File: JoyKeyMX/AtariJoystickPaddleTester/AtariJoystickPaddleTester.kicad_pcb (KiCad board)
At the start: 2 copper layers, 106.7 x 142.2 mm, 52 parts, among them J1 DB9_Male, J2 Barrel_Jack, SW1 SWITCH, U1 LM7809_TO220, U2 LM3914V, U3 LM3914V

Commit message: Route Atari Joystick and Paddle Tester
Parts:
- added G***: LOGO, Library:ScreamingLogo, F.Cu at (79.4, 87.6)
- added REF**: OSH_logo, Library:OSH_logo, F.Cu at (137.2, 168.8)
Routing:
- net 9V: track 0.00 -> 504.2 mm
- net GND: track 0.00 -> 238.8 mm, vias 0 -> 19
- net Net-(D11-Pad1): track 0.00 -> 197.8 mm
- net +9V: track 0.00 -> 185.4 mm
- net Net-(D10-Pad1): track 0.00 -> 180.4 mm
- net LEFT PADDLE & FIRE: track 0.00 -> 179.3 mm
- net Net-(D9-Pad1): track 0.00 -> 163.3 mm
- net Net-(D8-Pad1): track 0.00 -> 146.2 mm
- net Net-(D7-Pad1): track 0.00 -> 129.1 mm
- net 5V: track 0.00 -> 125.5 mm
- net Net-(D27-Pad1): track 0.00 -> 124.3 mm
- net RIGHT PADDLE & FIRE: track 0.00 -> 123.4 mm
- net Net-(D26-Pad1): track 0.00 -> 113.0 mm
- net Net-(D6-Pad1): track 0.00 -> 112.0 mm
- net Net-(D25-Pad1): track 0.00 -> 101.7 mm
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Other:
- board size 106.7 x 142.2 mm -> 106.7 x 144.8 mm
- board text added: "(c) Bertrand Le Roy 2022 https://github.com/bleroy/3d-junkyard/tree/main/JoyKeyMX https://atariage.com/forums/profile/76850-screamingattheradio/ https://www.twitch.tv/screamingattheradio https://www.youtube.com/channel/UCyaCK4oVWf1ty618W-MJcrg"
- board text added: "Atari Joystick and Paddle Tester"

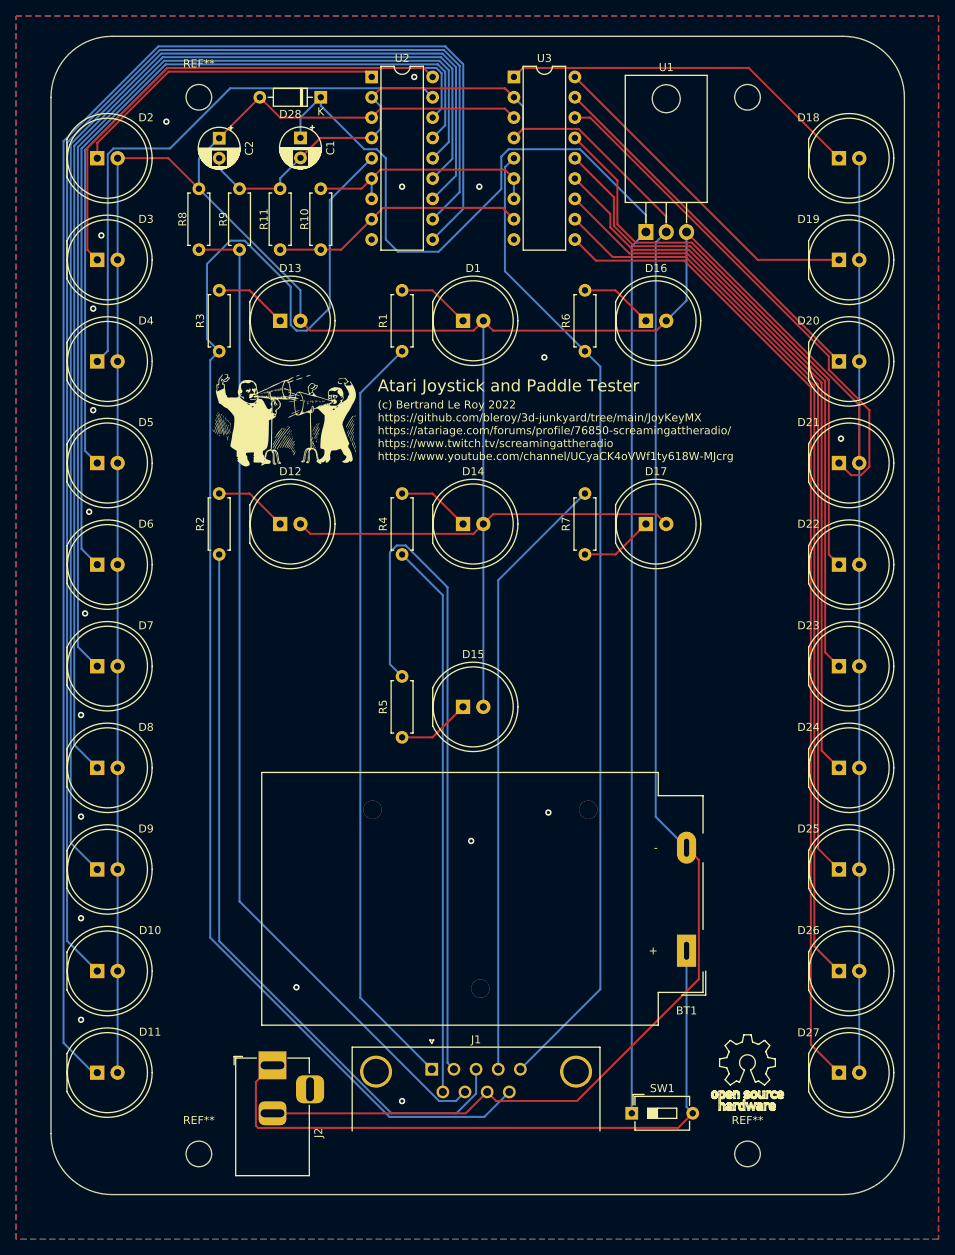
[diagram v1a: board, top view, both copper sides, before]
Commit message: Remove some unnecessary tracks.
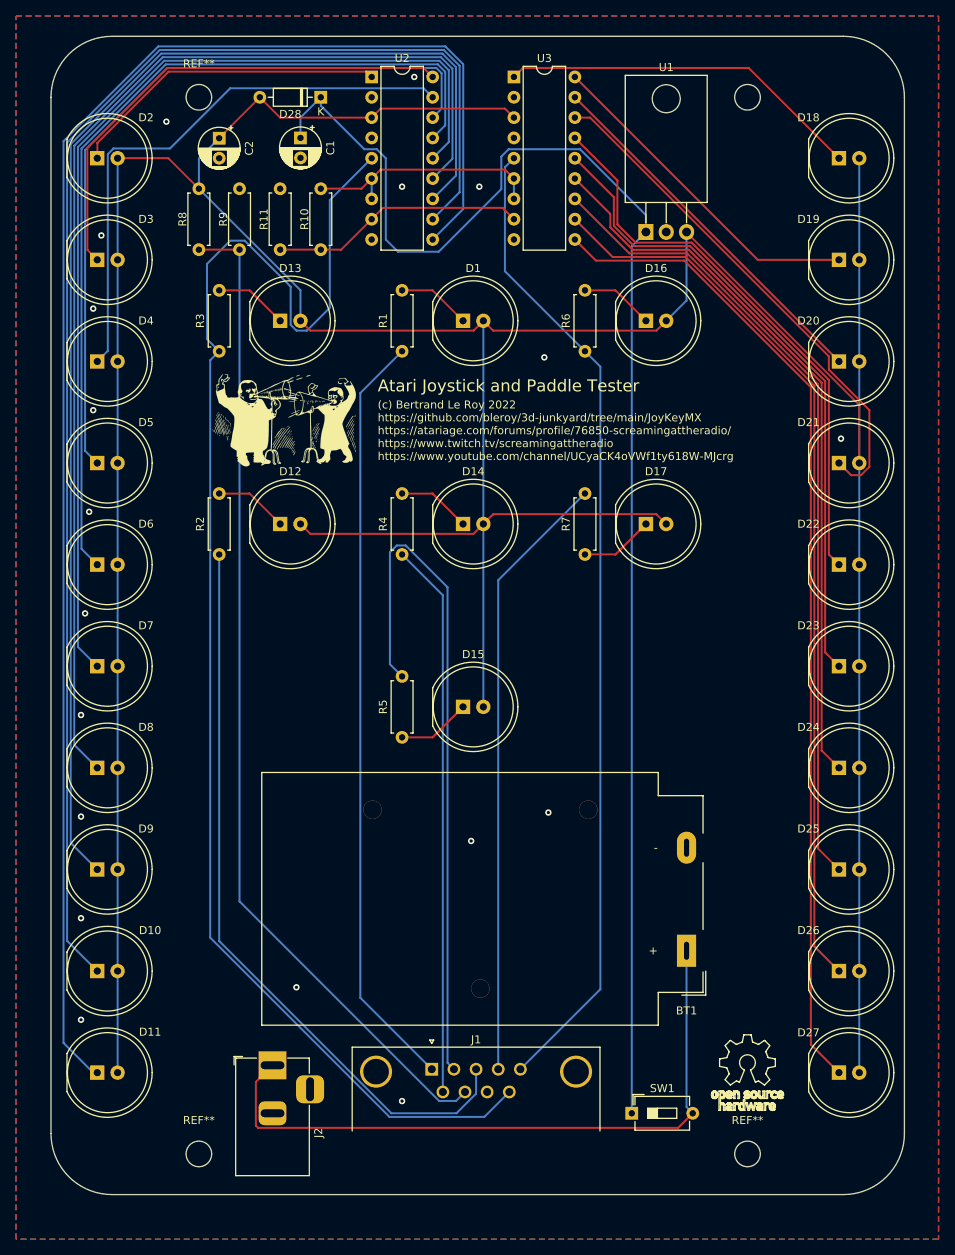
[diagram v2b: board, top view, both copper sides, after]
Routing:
- net GND: track 238.8 -> 0.00 mm
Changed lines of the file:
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@@
   (segment (start 83.82 49.31) (end 89.265489 54.755489) (width 0.25) (layer "B.Cu") (net 1))
   (segment (start 124.46 65.1) (end 122.692 66.868) (width 0.25) (layer "B.Cu") (net 1))
-  (segment (start 90.18 53.34) (end 83.78 53.34) (width 0.25) (layer "F.Cu") (net 2))
-  (segment (start 127 63.1697) (end 127 65.1) (width 0.25) (layer "F.Cu") (net 2))
-  (segment (start 101.949669 175.26) (end 104.615 172.594669) (width 0.25) (layer "F.Cu") (net 2))
-  (segment (start 131.069511 143.589511) (end 129.54 142.06) (width 0.25) (layer "F.Cu") (net 2))
-  (segment (start 116.045789 52.215489) (end 127 63.1697) (width 0.25) (layer "F.Cu") (net 2))
-  (segment (start 106.835489 47.135489) (end 107.96 48.26) (width 0.25) (layer "F.Cu") (net 2))
-  (segment (start 90.18 48.26) (end 91.304511 47.135489) (width 0.25) (layer "F.Cu") (net 2))
-  (segment (start 107.96 53.34) (end 109.084511 52.215489) (width 0.25) (layer "F.Cu") (net 2))
-  (segment (start 91.304511 47.135489) (end 106.835489 47.135489) (width 0.25) (layer "F.Cu") (net 2))
-  (segment (start 83.78 53.34) (end 81.28 55.84) (width 0.25) (layer "F.Cu") (net 2))
-  (segment (start 77.7825 175.26) (end 101.949669 175.26) (width 0.25) (layer "F.Cu") (net 2))
-  (segment (start 73.66 59.69) (end 78.74 59.69) (width 0.25) (layer "F.Cu") (net 2))
-  (segment (start 104.615 172.594669) (end 105.739511 173.71918) (width 0.25) (layer "F.Cu") (net 2))
-  (segment (start 109.084511 52.215489) (end 116.045789 52.215489) (width 0.25) (layer "F.Cu") (net 2))
-  (segment (start 105.739511 173.71918) (end 115.84082 173.71918) (width 0.25) (layer "F.Cu") (net 2))
-  (segment (start 115.84082 173.71918) (end 131.069511 158.490489) (width 0.25) (layer "F.Cu") (net 2))
-  (segment (start 131.069511 158.490489) (end 131.069511 143.589511) (width 0.25) (layer "F.Cu") (net 2))
   (via (at 93.98 173.736) (size 0.8) (drill 0.4) (layers "F.Cu" "B.Cu") (free) (net 2))
   (via (at 95.504 45.72) (size 0.8) (drill 0.4) (layers "F.Cu" "B.Cu") (free) (net 2))
@@
   (via (at 103.632 59.436) (size 0.8) (drill 0.4) (layers "F.Cu" "B.Cu") (free) (net 2))
   (via (at 53.848 150.876) (size 0.8) (drill 0.4) (layers "F.Cu" "B.Cu") (free) (net 2))
-  (segment (start 78.74 59.69) (end 78.74 58.38) (width 0.25) (layer "B.Cu") (net 2))
-  (segment (start 107.96 48.26) (end 109.084511 49.384511) (width 0.25) (layer "B.Cu") (net 2))
-  (segment (start 109.084511 49.384511) (end 109.084511 52.215489) (width 0.25) (layer "B.Cu") (net 2))
-  (segment (start 125.684511 66.415489) (end 127 65.1) (width 0.25) (layer "B.Cu") (net 2))
-  (segment (start 71.12 57.15) (end 73.66 59.69) (width 0.25) (layer "B.Cu") (net 2))
-  (segment (start 91.304511 52.215489) (end 90.18 53.34) (width 0.25) (layer "B.Cu") (net 2))
-  (segment (start 71.12 55.88) (end 71.12 57.15) (width 0.25) (layer "B.Cu") (net 2))
-  (segment (start 78.74 58.38) (end 81.28 55.84) (width 0.25) (layer "B.Cu") (net 2))
-  (segment (start 109.084511 52.215489) (end 107.96 53.34) (width 0.25) (layer "B.Cu") (net 2))
-  (segment (start 125.684511 138.204511) (end 125.684511 66.415489) (width 0.25) (layer "B.Cu") (net 2))
-  (segment (start 91.304511 49.384511) (end 91.304511 52.215489) (width 0.25) (layer "B.Cu") (net 2))
-  (segment (start 90.18 48.26) (end 91.304511 49.384511) (width 0.25) (layer "B.Cu") (net 2))
-  (segment (start 129.54 142.06) (end 125.684511 138.204511) (width 0.25) (layer "B.Cu") (net 2))
   (segment (start 102.915489 77.424511) (end 82.504511 77.424511) (width 0.25) (layer "F.Cu") (net 3))
   (segment (start 129.54 65.1475) (end 151.13 86.7375) (width 0.25) (layer "F.Cu") (net 3))

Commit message: Change switch footprint
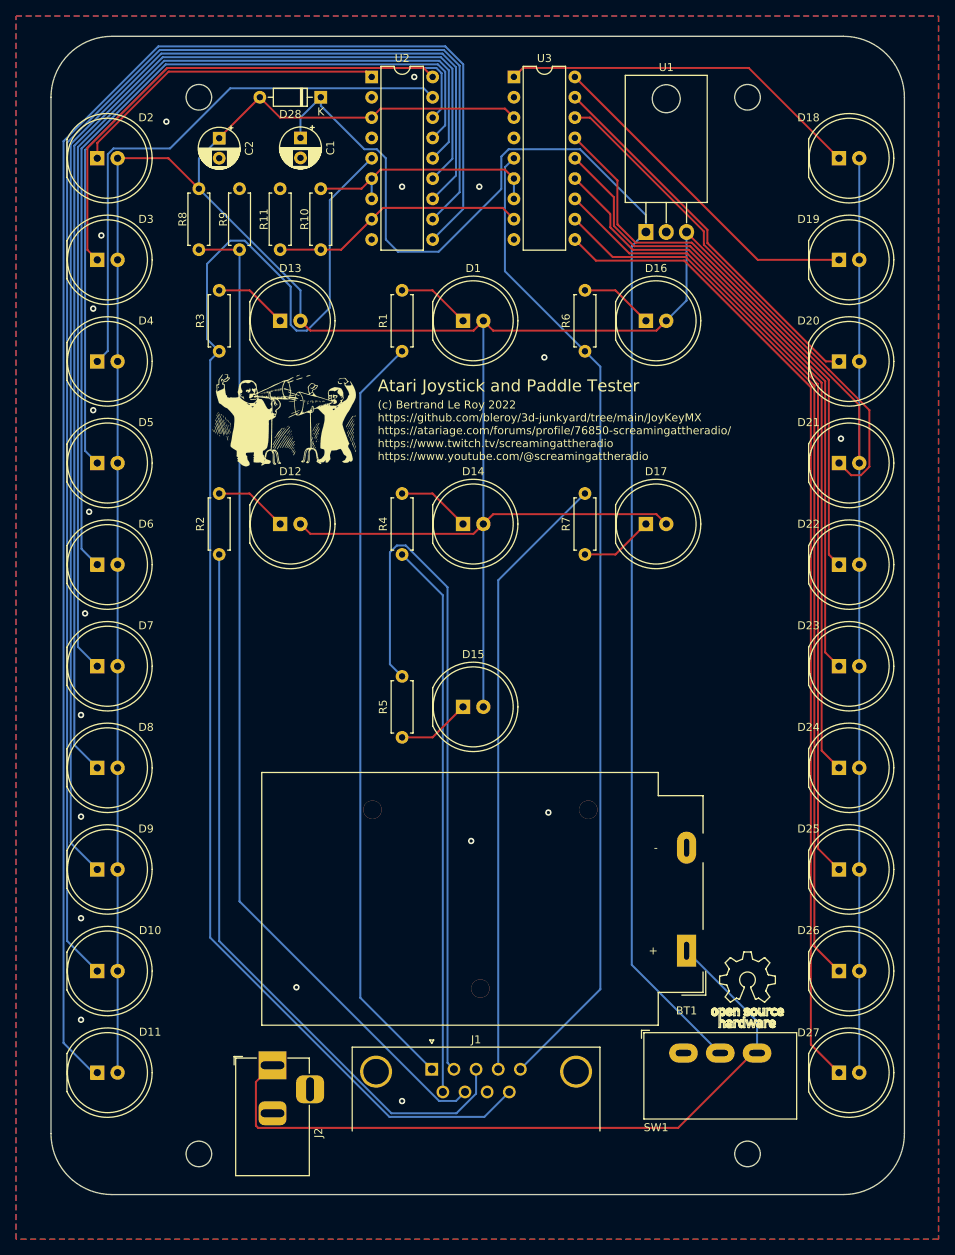
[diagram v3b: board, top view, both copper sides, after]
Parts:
- SW1: footprint Button_Switch_THT:SW_DIP_SPSTx01_Slide_6.7x4.1mm_W7.62mm_P2.54mm_LowProfile -> Library:Slide Switch 3-pin
- moved REF** 10.4 mm to (137.2, 158.5)
- moved SW1 9.92 mm to (129.2, 167.7)
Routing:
- net Net-(BT1-Pad1): track 84.5 -> 91.5 mm
- net +9V: track 185.4 -> 182.5 mm
- net Net-(D20-Pad1): track 46.7 -> 47.7 mm
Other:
- board text added: "(c) Bertrand Le Roy 2022 https://github.com/bleroy/3d-junkyard/tree/main/JoyKeyMX https://atariage.com/forums/profile/76850-screamingattheradio/ https://www.twitch.tv/screamingattheradio https://www.youtube.com/@screamingattheradio"
- board text removed: "(c) Bertrand Le Roy 2022 https://github.com/bleroy/3d-junkyard/tree/main/JoyKeyMX https://atariage.com/forums/profile/76850-screamingattheradio/ https://www.twitch.tv/screamingattheradio https://www.youtube.com/channel/UCyaCK4oVWf1ty618W-MJcrg"
